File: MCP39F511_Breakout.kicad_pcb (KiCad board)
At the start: 2 copper layers, 35.6 x 27.9 mm, 2 parts, among them J1 Conn_01x10, U1 MCP39F511-E_MQ

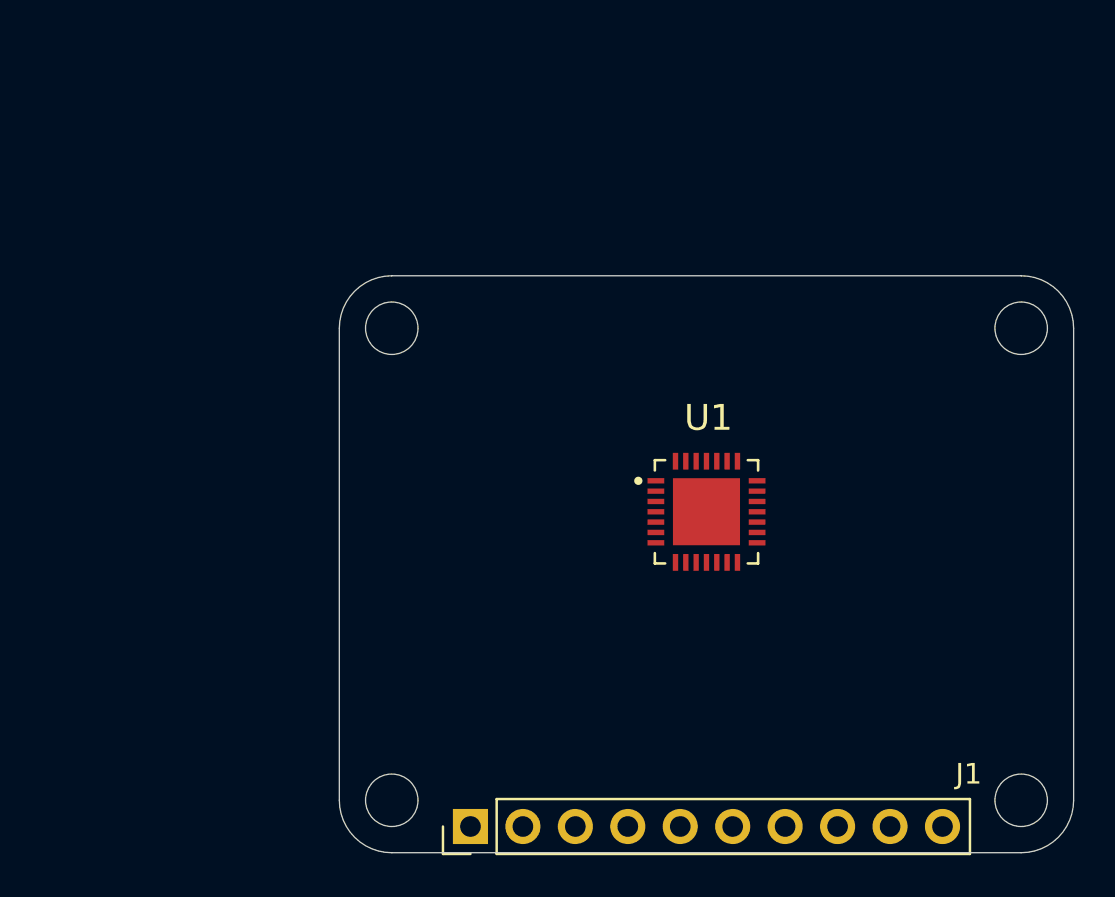
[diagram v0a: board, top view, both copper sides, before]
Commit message: Initial complete schematic
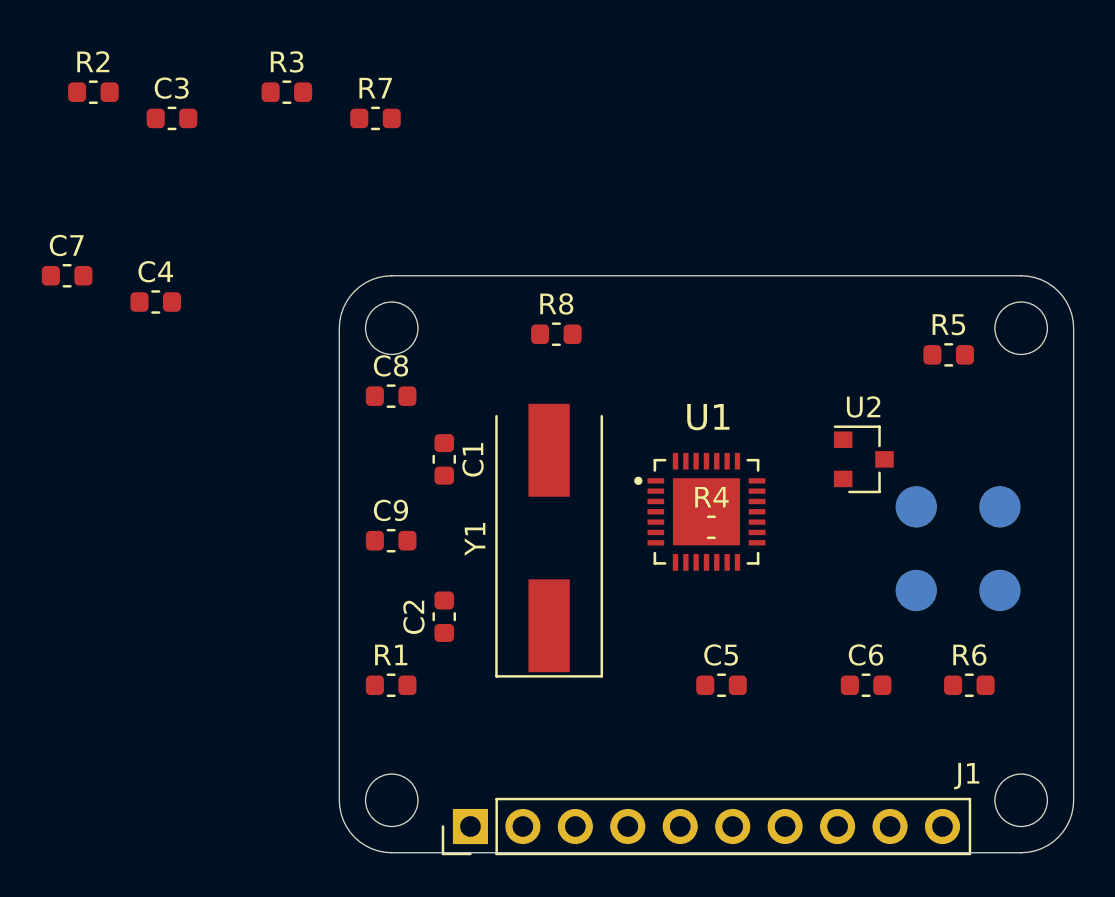
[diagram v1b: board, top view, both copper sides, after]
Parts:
- added C1: 22p, Capacitor_SMD:C_0603_1608Metric, F.Cu at (115.6, 99.1)
- added C2: 22p, Capacitor_SMD:C_0603_1608Metric, F.Cu at (115.6, 106.7)
- added C3: 100n, Capacitor_SMD:C_0603_1608Metric, F.Cu at (102.4, 82.5)
- added C4: 1u, Capacitor_SMD:C_0603_1608Metric, F.Cu at (101.6, 91.4)
- added C5: 100n, Capacitor_SMD:C_0603_1608Metric, F.Cu at (129.0, 110.0)
- added C6: 33n, Capacitor_SMD:C_0603_1608Metric, F.Cu at (136.0, 110.0)
- added C7: 33n, Capacitor_SMD:C_0603_1608Metric, F.Cu at (97.3, 90.2)
- added C8: 33n, Capacitor_SMD:C_0603_1608Metric, F.Cu at (113.0, 96.0)
- added C9: 33n, Capacitor_SMD:C_0603_1608Metric, F.Cu at (113.0, 103.0)
- added R1: 10R, Resistor_SMD:R_0603_1608Metric, F.Cu at (113.0, 110.0)
- added R2: 1K, Resistor_SMD:R_0603_1608Metric, F.Cu at (98.6, 81.3)
- added R3: 1K, Resistor_SMD:R_0603_1608Metric, F.Cu at (108.0, 81.3)
- added R4: 2.4R, Resistor_SMD:R_0603_1608Metric, F.Cu at (128.5, 102.4)
- added R5: 2.4R, Resistor_SMD:R_0603_1608Metric, F.Cu at (140.0, 94.0)
- added R6: 1K, Resistor_SMD:R_0603_1608Metric, F.Cu at (141.0, 110.0)
- added R7: 1K, Resistor_SMD:R_0603_1608Metric, F.Cu at (112.2, 82.5)
- added R8: 10K, Resistor_SMD:R_0603_1608Metric, F.Cu at (121.0, 93.0)
- added TP1: TestPoint, TestPoint:TestPoint_Pad_D2.0mm, B.Cu at (142.5, 101.4)
- added TP2: TestPoint, TestPoint:TestPoint_Pad_D2.0mm, B.Cu at (142.5, 105.4)
- added TP3: TestPoint, TestPoint:TestPoint_Pad_D2.0mm, B.Cu at (138.4, 105.4)
- added TP4: TestPoint, TestPoint:TestPoint_Pad_D2.0mm, B.Cu at (138.4, 101.4)
- added U2: MCP9700T-ETT, Package_TO_SOT_SMD:SOT-23, F.Cu at (135.9, 99.1)
- added Y1: Crystal, Crystal:Crystal_SMD_HC49-SD, F.Cu at (120.7, 102.9)
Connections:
- J1 pad 10: Net-(J1-Pad10) -> GND
- J1 pad 2: Net-(J1-Pad2) -> VP
- J1 pad 3: Net-(J1-Pad3) -> VN
- J1 pad 4: Net-(J1-Pad4) -> ~RESET
- J1 pad 5: Net-(J1-Pad5) -> PWM
- J1 pad 6: Net-(J1-Pad6) -> TX
- J1 pad 7: Net-(J1-Pad7) -> RX
- J1 pad 8: Net-(J1-Pad8) -> IP
- J1 pad 9: Net-(J1-Pad9) -> IN
- U1 pad 10: Net-(U1-Pad10) -> ~RESET
- U1 pad 12: Net-(U1-Pad12) -> TX
- U1 pad 13: Net-(U1-Pad13) -> Net-(U1-Pad5)
- U1 pad 14: Net-(U1-Pad14) -> PWM
- U1 pad 16: Net-(U1-Pad16) -> IIN+
- U1 pad 17: Net-(U1-Pad17) -> IIN-
- U1 pad 18: Net-(U1-Pad18) -> VIN-
- U1 pad 19: Net-(U1-Pad19) -> VIN+
- U1 pad 20: Net-(U1-Pad20) -> T_A
- U1 pad 21: Net-(U1-Pad21) -> GNDA
- U1 pad 24: Net-(U1-Pad24) -> GNDA
- U1 pad 25: Net-(U1-Pad25) -> +3V3
- U1 pad 27: Net-(U1-Pad24) -> GNDA
- U1 pad 29: Net-(U1-Pad29) -> GNDA
- U1 pad 4: Net-(U1-Pad4) -> RX
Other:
- net class Default removed

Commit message: Finish routing and silk-screens
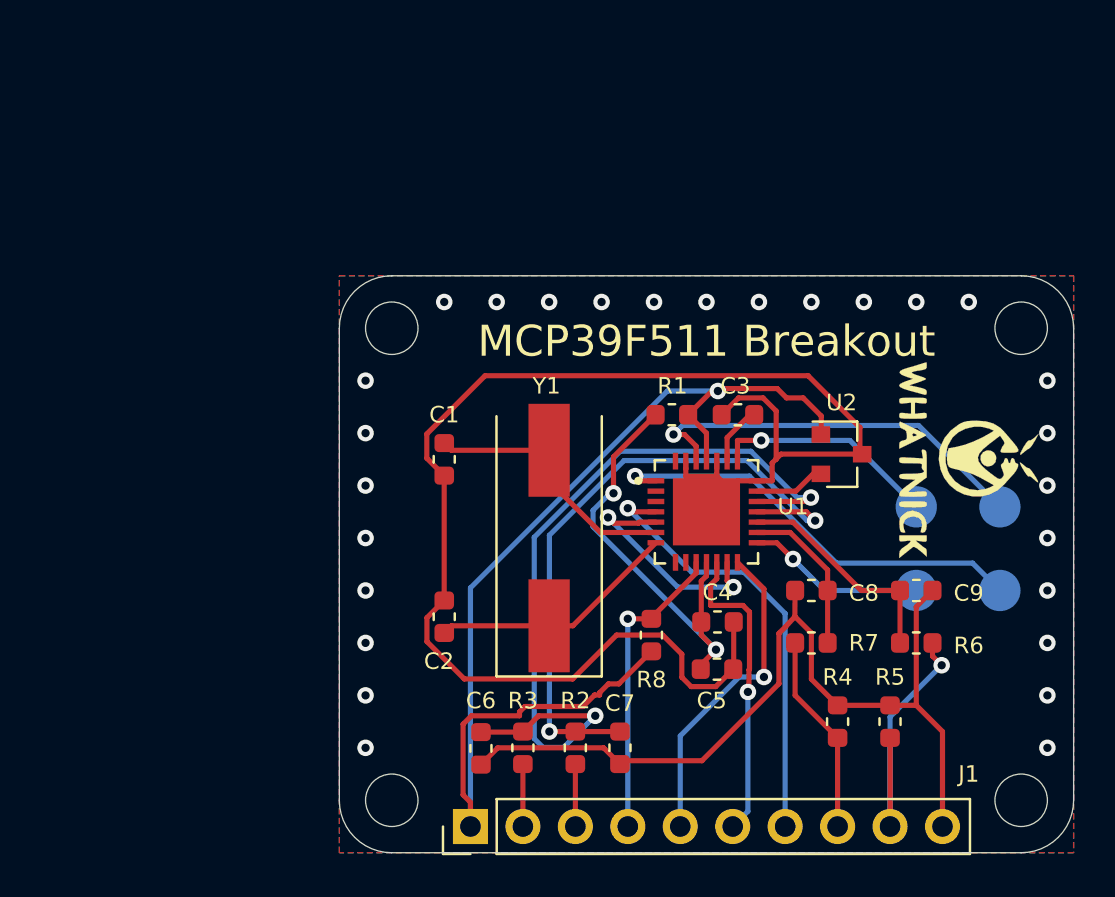
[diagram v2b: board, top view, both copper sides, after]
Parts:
- added LOGO1: Logo_Open_Hardware_Small, Symbol:OSHW-Logo2_7.3x6mm_SilkScreen, B.Cu at (128.8, 108.6)
- added LOGO2: LOGO, Whatnick_logo:Whatnick_logo, F.Cu at (141.0, 99.1)
- moved R2 39.4 mm to (121.9, 113.0), turned to -90 degrees
- moved C7 35.2 mm to (124.1, 113.0), turned to 90 degrees
- moved R3 33.7 mm to (119.4, 113.0), turned to -90 degrees
- moved R7 33.0 mm to (133.3, 108.0), turned to 180 degrees
- moved C4 31.3 mm to (128.8, 106.9)
- moved C3 30.9 mm to (129.8, 96.9), turned to 180 degrees
- moved C9 25.5 mm to (138.4, 105.4), turned to 180 degrees
- moved C8 22.4 mm to (133.3, 105.4), turned to 180 degrees
- moved C6 18.9 mm to (117.3, 113.1), turned to -90 degrees
- moved R1 18.9 mm to (126.6, 96.9)
- moved R5 18.0 mm to (137.2, 111.8), turned to 90 degrees
- moved R8 15.3 mm to (125.6, 107.6), turned to -90 degrees
- moved R4 11.2 mm to (134.6, 111.8), turned to -90 degrees
- moved R6 3.29 mm to (138.4, 108.0)
- moved U2 1.11 mm to (134.8, 98.8)
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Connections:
- C1 pad 2: GNDA -> GND
- C2 pad 2: GNDA -> GND
- C3 pad 2: GNDA -> GND
- C4 pad 2: GNDA -> GND
- C5 pad 2: GNDA -> GND
- U1 pad 21: GNDA -> GND
- U1 pad 24: GNDA -> GND
- U1 pad 27: GNDA -> GND
- U1 pad 29: GNDA -> GND
- U2 pad 3: GNDA -> GND
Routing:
- net GND: track 0.00 -> 118.0 mm, vias 0 -> 27
- net +3V3: track 0.00 -> 54.4 mm, vias 0 -> 1
- net VIN+: track 0.00 -> 38.1 mm, vias 0 -> 2
- net VIN-: track 0.00 -> 31.5 mm, vias 0 -> 2
- net RX: track 0.00 -> 21.5 mm, vias 0 -> 1
- net Net-(C4-Pad1): track 0.00 -> 21.1 mm, vias 0 -> 2
- net Net-(TP2-Pad1): track 0.00 -> 21.1 mm, vias 0 -> 1
- net Net-(TP1-Pad1): track 0.00 -> 19.7 mm, vias 0 -> 1
- net PWM: track 0.00 -> 15.7 mm, vias 0 -> 1
- net TX: track 0.00 -> 14.9 mm, vias 0 -> 1
- net ~RESET: track 0.00 -> 14.8 mm, vias 0 -> 1
- net IN: track 0.00 -> 14.4 mm, vias 0 -> 1
- net Net-(C1-Pad1): track 0.00 -> 12.9 mm
- net Net-(C2-Pad1): track 0.00 -> 12.1 mm
- net Net-(U1-Pad13): track 0.00 -> 11.2 mm, vias 0 -> 2
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- added copper zone on B.Cu, net GND
- added copper zone on F.Cu, net GND
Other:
- board text added: "MCP39F511 Breakout"
- board text added: "by Tisham Dhar http://whatnick.com v0.1 16/11/2020"

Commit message: Add gerbers
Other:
- board text added: "3V3"
- board text added: "GND"
- board text added: "IN"
- board text added: "IP"
- board text added: "PWM"
- board text added: "RX"
- board text added: "TX"
- board text added: "VN"
- board text added: "VP"
- board text added: "~RESET"
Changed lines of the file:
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@@
       (layerselection 0x00010fc_ffffffff)
       (disableapertmacros false)
-      (usegerberextensions false)
+      (usegerberextensions true)
       (usegerberattributes false)
       (usegerberadvancedattributes false)
@@
       (viasonmask false)
       (mode 1)
-      (useauxorigin false)
+      (useauxorigin true)
       (hpglpennumber 1)
       (hpglpenspeed 20)
@@
       (outputformat 1)
       (mirror false)
-      (drillshape 1)
+      (drillshape 0)
       (scaleselection 1)
-      (outputdirectory "")
+      (outputdirectory "gerbers")
     )
   )
@@
   (gr_circle (center 113.03 115.57) (end 111.76 115.57) (layer "Edge.Cuts") (width 0.05))
   (gr_line (start 143.51 118.11) (end 113.03 118.11) (layer "Edge.Cuts") (width 0.05))
+  (gr_text "GND" (at 139.7 113.752381 90) (layer "B.SilkS")
+    (effects (font (size 1 1) (thickness 0.2)) (justify mirror))
+  )
+  (gr_text "IN" (at 137.16 114.514285 90) (layer "B.SilkS")
+    (effects (font (size 1 1) (thickness 0.2)) (justify mirror))
+  )
+  (gr_text "~RESET" (at 124.587 113.014285 90) (layer "B.SilkS")
+    (effects (font (size 1 1) (thickness 0.2)) (justify mirror))
+  )
+  (gr_text "3V3" (at 116.84 113.895238 90) (layer "B.SilkS")
+    (effects (font (size 1 1) (thickness 0.2)) (justify mirror))
+  )
   (gr_text "by Tisham Dhar\nhttp://whatnick.com\nv0.1 16/11/2020" (at 128.905 94.615) (layer "B.SilkS")
-    (effects (font (size 1 1) (thickness 0.15)) (justify mirror))
+    (effects (font (size 1 1) (thickness 0.25)) (justify mirror))
+  )
+  (gr_text "VN" (at 121.92 114.323809 90) (layer "B.SilkS")
+    (effects (font (size 1 1) (thickness 0.2)) (justify mirror))
+  )
+  (gr_text "TX" (at 129.54 114.419047 90) (layer "B.SilkS")
+    (effects (font (size 1 1) (thickness 0.2)) (justify mirror))
+  )
+  (gr_text "PWM" (at 127 113.633333 90) (layer "B.SilkS")
+    (effects (font (size 1 1) (thickness 0.2)) (justify mirror))
+  )
+  (gr_text "VP" (at 119.507 114.347619 90) (layer "B.SilkS")
+    (effects (font (size 1 1) (thickness 0.2)) (justify mirror))
+  )
+  (gr_text "IP" (at 134.62 114.538095 90) (layer "B.SilkS")
+    (effects (font (size 1 1) (thickness 0.2)) (justify mirror))
+  )
+  (gr_text "RX" (at 132.08 114.3 90) (layer "B.SilkS")
+    (effects (font (size 1 1) (thickness 0.2)) (justify mirror))
   )
   (gr_text "MCP39F511 Breakout\n" (at 128.27 93.345) (layer "F.SilkS")

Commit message: Update BOM
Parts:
- Y1: value Crystal -> 4MHz / 16pF
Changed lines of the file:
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@@
     (property "Sheet file" "C:/Users/Tisham/Documents/kicad/MCP39F511_Breakout/MCP39F511_Breakout.kicad_sch")
     (property "Sheet name" "")
+    (property "manf#" "MCP39F511-E/MQ")
     (attr through_hole)
     (fp_text reference "U1" (at 4.191 -0.254) (layer "F.SilkS")
@@
     (property "Sheet file" "C:/Users/Tisham/Documents/kicad/MCP39F511_Breakout/MCP39F511_Breakout.kicad_sch")
     (property "Sheet name" "")
+    (property "manf#" "C0603C105K4PAC7411")
     (attr smd)
     (fp_text reference "C4" (at 0 -1.43) (layer "F.SilkS")
@@
     (property "Sheet file" "C:/Users/Tisham/Documents/kicad/MCP39F511_Breakout/MCP39F511_Breakout.kicad_sch")
     (property "Sheet name" "")
-    (property "manf#" "06035C273MAT2A")
+    (property "manf#" "0603YC333KAT2A")
     (attr smd)
     (fp_text reference "C8" (at -2.54 -0.127) (layer "F.SilkS")
@@
     (property "Sheet file" "C:/Users/Tisham/Documents/kicad/MCP39F511_Breakout/MCP39F511_Breakout.kicad_sch")
     (property "Sheet name" "")
+    (property "manf#" "MCP9700T-E/TT")
     (attr smd)
     (fp_text reference "U2" (at 0 -2.5) (layer "F.SilkS")
@@
     (descr "Through hole straight pin header, 1x10, 2.54mm pitch, single row")
     (tags "Through hole pin header THT 1x10 2.54mm single row")
-    (property "DNP" " ")
+    (property "DNP" "...")
     (property "Sheet file" "C:/Users/Tisham/Documents/kicad/MCP39F511_Breakout/MCP39F511_Breakout.kicad_sch")
     (property "Sheet name" "")
@@
     (property "Sheet file" "C:/Users/Tisham/Documents/kicad/MCP39F511_Breakout/MCP39F511_Breakout.kicad_sch")
     (property "Sheet name" "")
+    (property "manf#" "C0603C220M4RACTU")
     (attr smd)
     (fp_text reference "C1" (at -2.159 0 180) (layer "F.SilkS")
@@
     (property "Sheet file" "C:/Users/Tisham/Documents/kicad/MCP39F511_Breakout/MCP39F511_Breakout.kicad_sch")
     (property "Sheet name" "")
-    (property "manf#" "06035C273MAT2A")
+    (property "manf#" "0603YC333KAT2A")
     (attr smd)
     (fp_text reference "C7" (at 2.159 0 180) (layer "F.SilkS")
@@
   (module "Whatnick_logo:Whatnick_logo" (layer "F.Cu")
     (at 140.97 99.06 -90)
+    (property "DNP" "...")
     (property "Sheet file" "C:/Users/Tisham/Documents/kicad/MCP39F511_Breakout/MCP39F511_Breakout.kicad_sch")
     (property "Sheet name" "")
@@
     (property "Sheet file" "C:/Users/Tisham/Documents/kicad/MCP39F511_Breakout/MCP39F511_Breakout.kicad_sch")
     (property "Sheet name" "")
+    (property "manf#" "C0603C104K4PACTU")
     (attr smd)
     (fp_text reference "C5" (at -0.254 1.524) (layer "F.SilkS")
@@
     (property "Sheet file" "C:/Users/Tisham/Documents/kicad/MCP39F511_Breakout/MCP39F511_Breakout.kicad_sch")
     (property "Sheet name" "")
+    (property "manf#" "C0603C220M4RACTU")
     (attr smd)
     (fp_text reference "C2" (at -2.159 -0.254 180) (layer "F.SilkS")
@@
     (property "Sheet file" "C:/Users/Tisham/Documents/kicad/MCP39F511_Breakout/MCP39F511_Breakout.kicad_sch")
     (property "Sheet name" "")
-    (property "manf#" "06035C273MAT2A")
+    (property "manf#" "0603YC333KAT2A")
     (attr smd)
     (fp_text reference "C9" (at -2.54 -0.127) (layer "F.SilkS")
@@
     (property "Sheet file" "C:/Users/Tisham/Documents/kicad/MCP39F511_Breakout/MCP39F511_Breakout.kicad_sch")
     (property "Sheet name" "")
+    (property "manf#" "C0603C104K4PACTU")
     (attr smd)
     (fp_text reference "C3" (at 0.127 1.397) (layer "F.SilkS")
@@
     (property "Sheet file" "C:/Users/Tisham/Documents/kicad/MCP39F511_Breakout/MCP39F511_Breakout.kicad_sch")
     (property "Sheet name" "")
-    (property "manf#" "06035C273MAT2A")
+    (property "manf#" "0603YC333KAT2A")
     (attr smd)
     (fp_text reference "C6" (at -2.3115 0 180) (layer "F.SilkS")
@@
     (property "Sheet file" "C:/Users/Tisham/Documents/kicad/MCP39F511_Breakout/MCP39F511_Breakout.kicad_sch")
     (property "Sheet name" "")
+    (property "manf#" "RC0603FR-0710RP")
     (attr smd)
     (fp_text reference "R1" (at 0.0255 -1.397) (layer "F.SilkS")
@@
     (property "Sheet file" "C:/Users/Tisham/Documents/kicad/MCP39F511_Breakout/MCP39F511_Breakout.kicad_sch")
     (property "Sheet name" "")
+    (property "manf#" "LFXTAL003071Reel")
     (attr smd)
     (fp_text reference "Y1" (at 7.366 -0.127 180) (layer "F.SilkS")
       (effects (font (size 0.8 0.8) (thickness 0.2)))
     )
-    (fp_text value "Crystal" (at 0 3.55 90) (layer "F.Fab")
+    (fp_text value "4MHz / 16pF" (at 0 3.55 90) (layer "F.Fab")
       (effects (font (size 1 1) (thickness 0.15)))
     )
@@
     (property "Sheet file" "C:/Users/Tisham/Documents/kicad/MCP39F511_Breakout/MCP39F511_Breakout.kicad_sch")
     (property "Sheet name" "")
+    (property "manf#" "RC0603FR-0710KL")
     (attr smd)
     (fp_text reference "R8" (at 2.159 0 180) (layer "F.SilkS")
@@
     (descr "Open Source Hardware Symbol")
     (tags "Logo Symbol OSHW")
+    (property "DNP" "...")
     (property "Sheet file" "C:/Users/Tisham/Documents/kicad/MCP39F511_Breakout/MCP39F511_Breakout.kicad_sch")
     (property "Sheet name" "")
@@
     (descr "SMD pad as test Point, diameter 2.0mm")
     (tags "test point SMD pad")
+    (property "DNP" "...")
     (property "Sheet file" "C:/Users/Tisham/Documents/kicad/MCP39F511_Breakout/MCP39F511_Breakout.kicad_sch")
     (property "Sheet name" "")
@@
     (descr "SMD pad as test Point, diameter 2.0mm")
     (tags "test point SMD pad")
+    (property "DNP" "...")
     (property "Sheet file" "C:/Users/Tisham/Documents/kicad/MCP39F511_Breakout/MCP39F511_Breakout.kicad_sch")
     (property "Sheet name" "")
@@
     (descr "SMD pad as test Point, diameter 2.0mm")
     (tags "test point SMD pad")
+    (property "DNP" "...")
     (property "Sheet file" "C:/Users/Tisham/Documents/kicad/MCP39F511_Breakout/MCP39F511_Breakout.kicad_sch")
     (property "Sheet name" "")
@@
     (descr "SMD pad as test Point, diameter 2.0mm")
     (tags "test point SMD pad")
-    (property "Sheet file" "C:/Users/Tisham/Documents/kicad/MCP39F511_Breakout/MCP39F511_Breakout.kicad_sch")
-    (property "Sheet name" "")
+    (property "DNP" "...")
+    (property "Sheet file" "C:/Users/Tisham/Documents/kicad/MCP39F511_Breakout/MCP39F511_Breakout.kicad_sch")
+    (property "Sheet name" "")
